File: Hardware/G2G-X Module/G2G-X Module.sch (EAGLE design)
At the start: 3 parts, among them J1 GROVE-4P-2.0-3470130P1

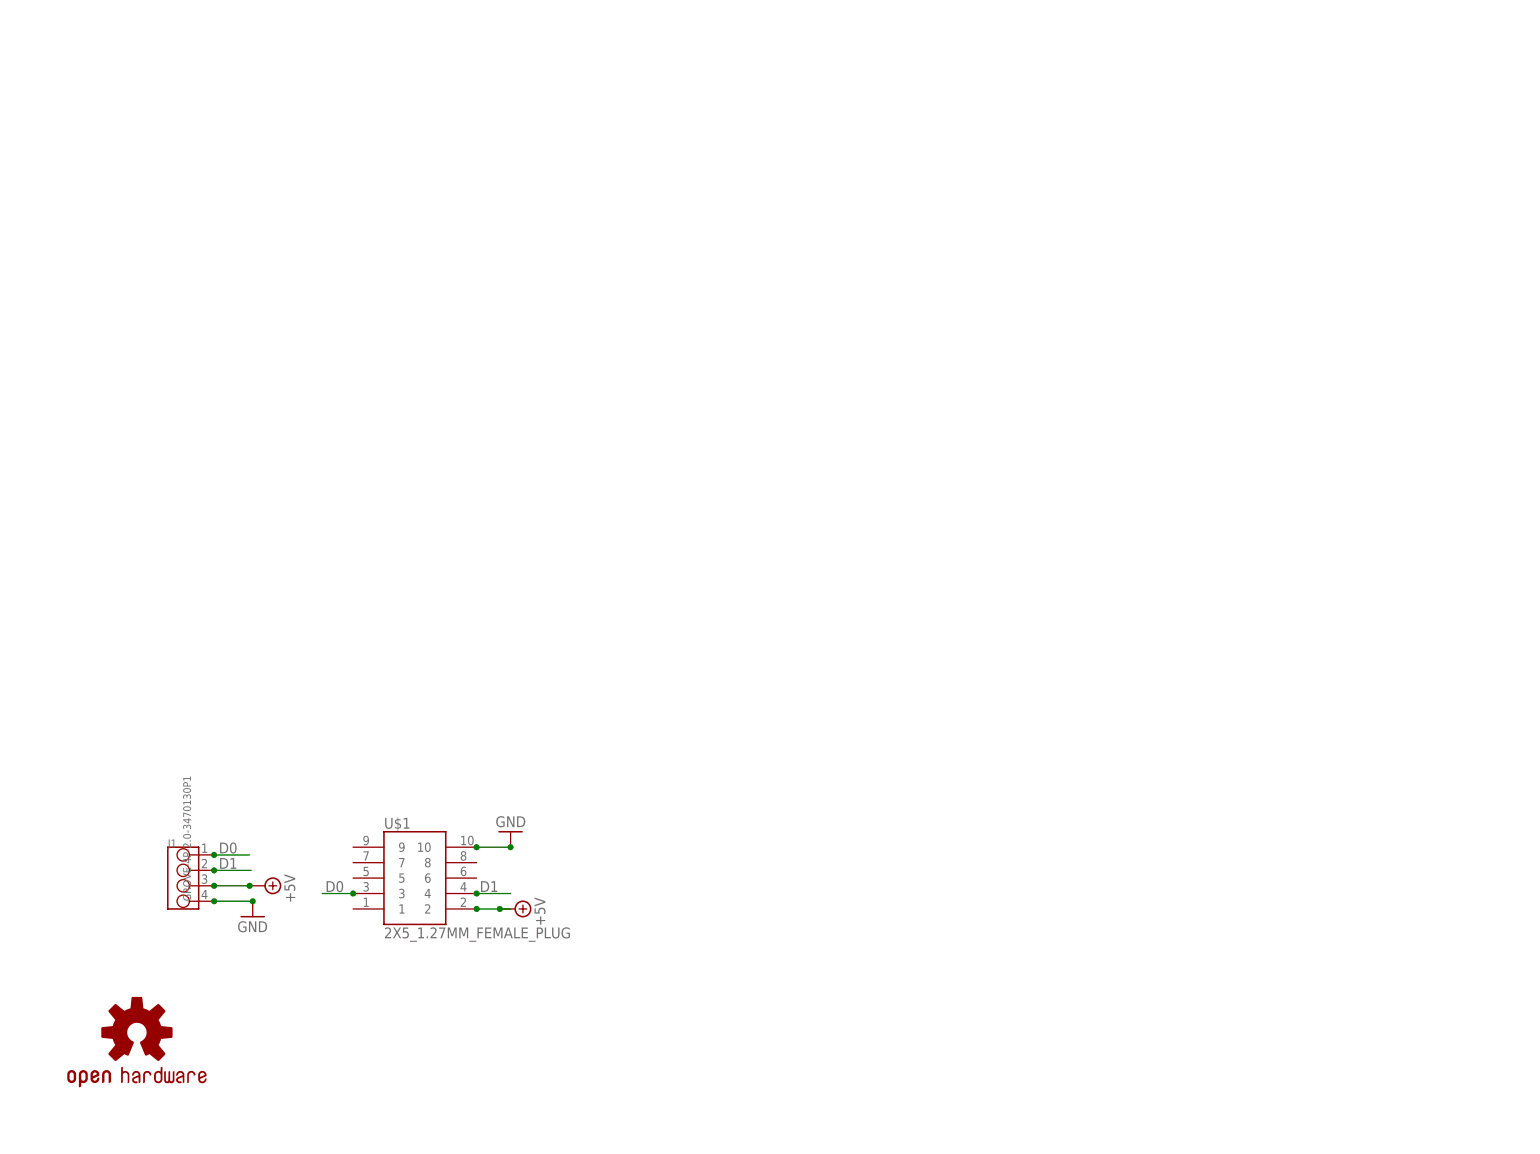
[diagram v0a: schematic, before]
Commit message: Added frames to the U and X module schematics.
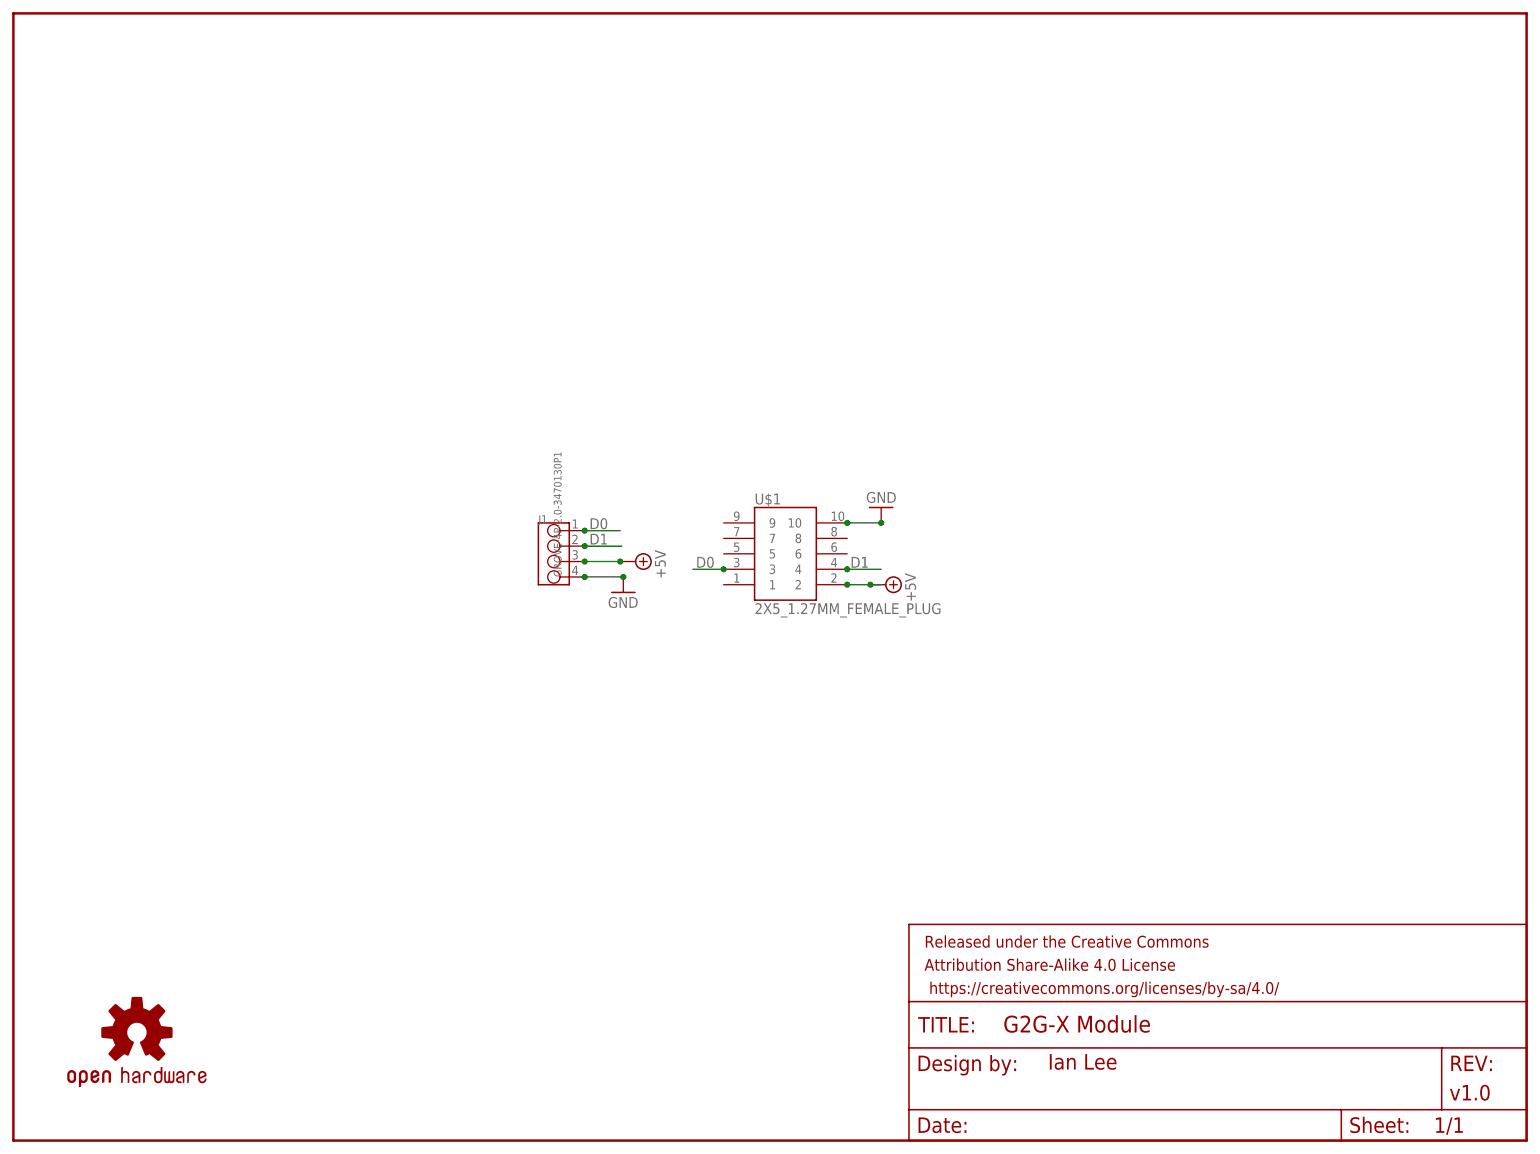
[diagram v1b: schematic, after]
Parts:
- added FRAME1: (no value), SparkFun-Aesthetics:FRAME-LETTERNO_PACKAGE
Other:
- moved on the sheet: J1, U$1
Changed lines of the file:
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@@
 <part name="SUPPLY1" library="supply2" deviceset="+5V" device=""/>
 <part name="SUPPLY2" library="supply2" deviceset="+5V" device=""/>
+<part name="FRAME1" library="SparkFun-Aesthetics" deviceset="FRAME-LETTER" device="NO_PACKAGE">
+<attribute name="DESIGNER" value="Ian Lee"/>
+<attribute name="VERSION" value="v1.0"/>
+</part>
 </parts>
 <sheets>
@@
 </plain>
 <instances>
-<instance part="J1" gate="J" x="27.94" y="43.18"/>
-<instance part="U$1" gate="G$1" x="66.04" y="43.18"/>
+<instance part="J1" gate="J" x="88.9" y="96.52"/>
+<instance part="U$1" gate="G$1" x="127" y="96.52"/>
 <instance part="LOGO1" gate="G$1" x="20.32" y="17.78"/>
-<instance part="GND1" gate="1" x="39.37" y="36.83"/>
-<instance part="GND2" gate="1" x="81.788" y="50.8" rot="R180"/>
-<instance part="SUPPLY1" gate="+5V" x="41.402" y="41.91" rot="R270"/>
-<instance part="SUPPLY2" gate="+5V" x="82.55" y="38.1" rot="R270"/>
+<instance part="GND1" gate="1" x="100.33" y="90.17"/>
+<instance part="GND2" gate="1" x="142.748" y="104.14" rot="R180"/>
+<instance part="SUPPLY1" gate="+5V" x="102.362" y="95.25" rot="R270"/>
+<instance part="SUPPLY2" gate="+5V" x="143.51" y="91.44" rot="R270"/>
+<instance part="FRAME1" gate="G$1" x="0" y="0"/>
+<instance part="FRAME1" gate="V" x="147.32" y="0"/>
 </instances>
 <busses>
@@
 <net name="GND" class="0">
 <segment>
-<wire x1="75.946" y1="48.26" x2="76.2" y2="48.26" width="0.1524" layer="91"/>
+<wire x1="136.906" y1="101.6" x2="137.16" y2="101.6" width="0.1524" layer="91"/>
 <pinref part="U$1" gate="G$1" pin="10"/>
-<junction x="76.2" y="48.26"/>
-<wire x1="76.2" y1="48.26" x2="81.788" y2="48.26" width="0.1524" layer="91"/>
+<junction x="137.16" y="101.6"/>
+<wire x1="137.16" y1="101.6" x2="142.748" y2="101.6" width="0.1524" layer="91"/>
 <pinref part="GND2" gate="1" pin="GND"/>
-<junction x="81.788" y="48.26"/>
+<junction x="142.748" y="101.6"/>
 </segment>
 <segment>
-<wire x1="32.766" y1="39.37" x2="33.02" y2="39.37" width="0.1524" layer="91"/>
+<wire x1="93.726" y1="92.71" x2="93.98" y2="92.71" width="0.1524" layer="91"/>
 <pinref part="J1" gate="J" pin="4"/>
-<junction x="33.02" y="39.37"/>
-<wire x1="33.02" y1="39.37" x2="39.37" y2="39.37" width="0.1524" layer="91"/>
+<junction x="93.98" y="92.71"/>
+<wire x1="93.98" y1="92.71" x2="100.33" y2="92.71" width="0.1524" layer="91"/>
 <pinref part="GND1" gate="1" pin="GND"/>
-<junction x="39.37" y="39.37"/>
+<junction x="100.33" y="92.71"/>
 </segment>
 </net>
 <net name="+5V" class="0">
 <segment>
-<wire x1="33.02" y1="41.91" x2="38.862" y2="41.91" width="0.1524" layer="91"/>
+<wire x1="93.98" y1="95.25" x2="99.822" y2="95.25" width="0.1524" layer="91"/>
 <pinref part="J1" gate="J" pin="3"/>
-<junction x="33.02" y="41.91"/>
-<wire x1="38.862" y1="41.91" x2="39.116" y2="41.91" width="0.1524" layer="91"/>
-<wire x1="32.512" y1="41.91" x2="33.02" y2="41.91" width="0.1524" layer="91"/>
+<junction x="93.98" y="95.25"/>
+<wire x1="99.822" y1="95.25" x2="100.076" y2="95.25" width="0.1524" layer="91"/>
+<wire x1="93.472" y1="95.25" x2="93.98" y2="95.25" width="0.1524" layer="91"/>
 <pinref part="SUPPLY1" gate="+5V" pin="+5V"/>
-<junction x="38.862" y="41.91"/>
+<junction x="99.822" y="95.25"/>
 </segment>
 <segment>
 <pinref part="U$1" gate="G$1" pin="2"/>
-<wire x1="81.788" y1="38.1" x2="80.01" y2="38.1" width="0.1524" layer="91"/>
-<junction x="76.2" y="38.1"/>
+<wire x1="142.748" y1="91.44" x2="140.97" y2="91.44" width="0.1524" layer="91"/>
+<junction x="137.16" y="91.44"/>
 <pinref part="SUPPLY2" gate="+5V" pin="+5V"/>
-<wire x1="80.01" y1="38.1" x2="76.2" y2="38.1" width="0.1524" layer="91"/>
-<junction x="80.01" y="38.1"/>
+<wire x1="140.97" y1="91.44" x2="137.16" y2="91.44" width="0.1524" layer="91"/>
+<junction x="140.97" y="91.44"/>
 </segment>
 </net>
@@
 <segment>
 <pinref part="J1" gate="J" pin="2"/>
-<wire x1="32.512" y1="44.45" x2="33.02" y2="44.45" width="0.1524" layer="91"/>
-<wire x1="33.02" y1="44.45" x2="39.116" y2="44.45" width="0.1524" layer="91"/>
-<junction x="33.02" y="44.45"/>
-<label x="33.782" y="44.704" size="1.778" layer="95"/>
+<wire x1="93.472" y1="97.79" x2="93.98" y2="97.79" width="0.1524" layer="91"/>
+<wire x1="93.98" y1="97.79" x2="100.076" y2="97.79" width="0.1524" layer="91"/>
+<junction x="93.98" y="97.79"/>
+<label x="94.742" y="98.044" size="1.778" layer="95"/>
 </segment>
 <segment>
 <pinref part="U$1" gate="G$1" pin="4"/>
-<wire x1="76.2" y1="40.64" x2="81.788" y2="40.64" width="0.1524" layer="91"/>
-<junction x="76.2" y="40.64"/>
-<label x="76.708" y="40.894" size="1.778" layer="95"/>
+<wire x1="137.16" y1="93.98" x2="142.748" y2="93.98" width="0.1524" layer="91"/>
+<junction x="137.16" y="93.98"/>
+<label x="137.668" y="94.234" size="1.778" layer="95"/>
 </segment>
 </net>
@@
 <segment>
 <pinref part="U$1" gate="G$1" pin="3"/>
-<wire x1="55.88" y1="40.64" x2="50.8" y2="40.64" width="0.1524" layer="91"/>
-<label x="51.308" y="40.894" size="1.778" layer="95"/>
-<junction x="55.88" y="40.64"/>
+<wire x1="116.84" y1="93.98" x2="111.76" y2="93.98" width="0.1524" layer="91"/>
+<label x="112.268" y="94.234" size="1.778" layer="95"/>
+<junction x="116.84" y="93.98"/>
 </segment>
 <segment>
 <pinref part="J1" gate="J" pin="1"/>
-<wire x1="33.02" y1="46.99" x2="38.862" y2="46.99" width="0.1524" layer="91"/>
-<junction x="33.02" y="46.99"/>
-<label x="33.782" y="47.244" size="1.778" layer="95"/>
+<wire x1="93.98" y1="100.33" x2="99.822" y2="100.33" width="0.1524" layer="91"/>
+<junction x="93.98" y="100.33"/>
+<label x="94.742" y="100.584" size="1.778" layer="95"/>
 </segment>
 </net>

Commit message: Replaced all 'G' logos with a new part for the logo.
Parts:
- added U$2: GADGETEER_LOGO_SMALL, SoftDust:GADGETEER_LOGO_SMALL
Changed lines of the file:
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@@
 <attribute name="VERSION" value="v1.0"/>
 </part>
+<part name="U$2" library="SoftDust" deviceset="GADGETEER_LOGO_SMALL" device=""/>
 </parts>
 <sheets>
@@
 <instance part="FRAME1" gate="G$1" x="0" y="0"/>
 <instance part="FRAME1" gate="V" x="147.32" y="0"/>
+<instance part="U$2" gate="G$1" x="43.18" y="10.16"/>
 </instances>
 <busses>
